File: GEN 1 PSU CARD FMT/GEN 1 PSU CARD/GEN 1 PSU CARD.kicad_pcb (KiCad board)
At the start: 4 copper layers, 245.3 x 107.1 mm, 15 parts, among them J2 1935226, J3 1935226, J4 39-28-1243, U1 ProMicro

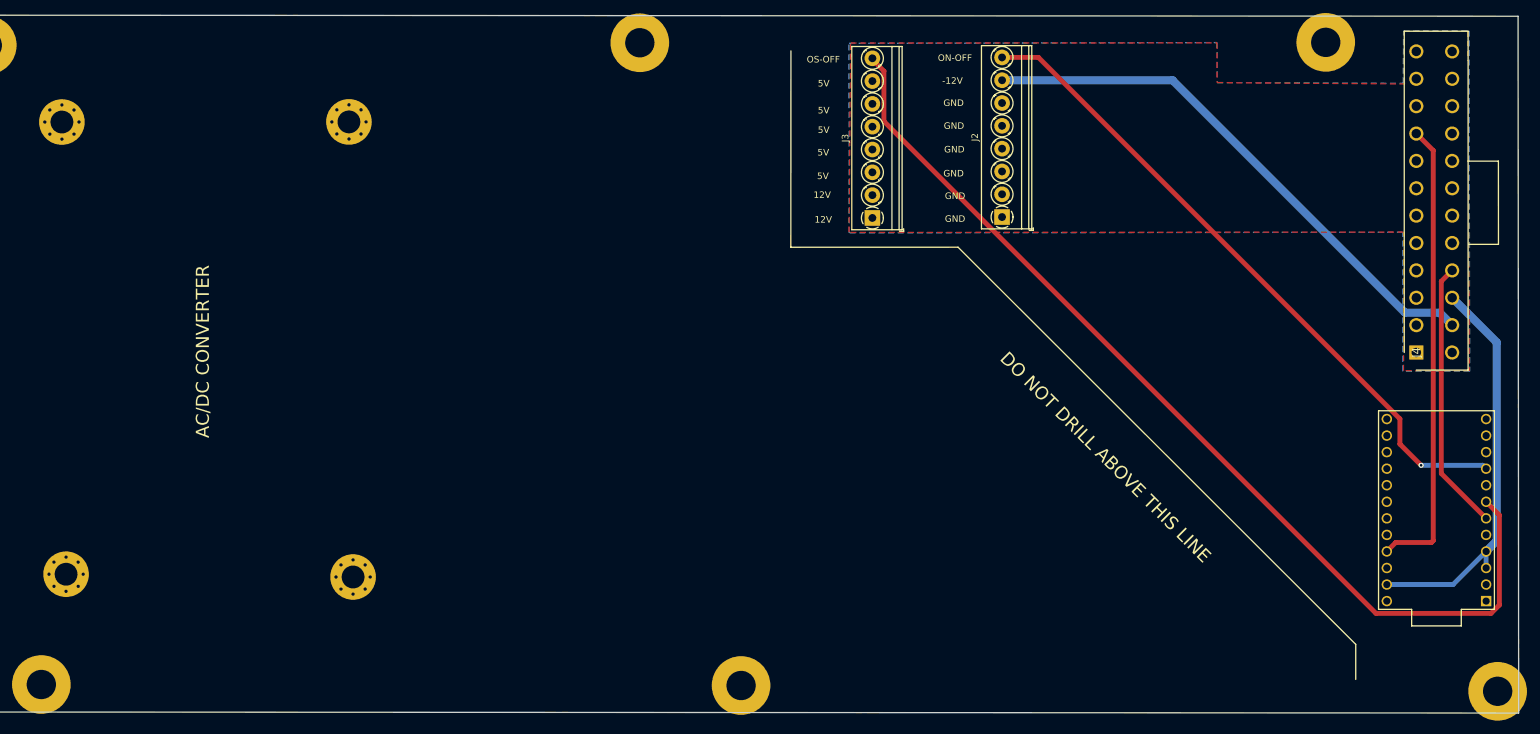
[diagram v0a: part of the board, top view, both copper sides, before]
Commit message: Gen 1 Card update
-Revised Gen1 card and added high power ACDC converter footprint and repositioned components so it's two layer.
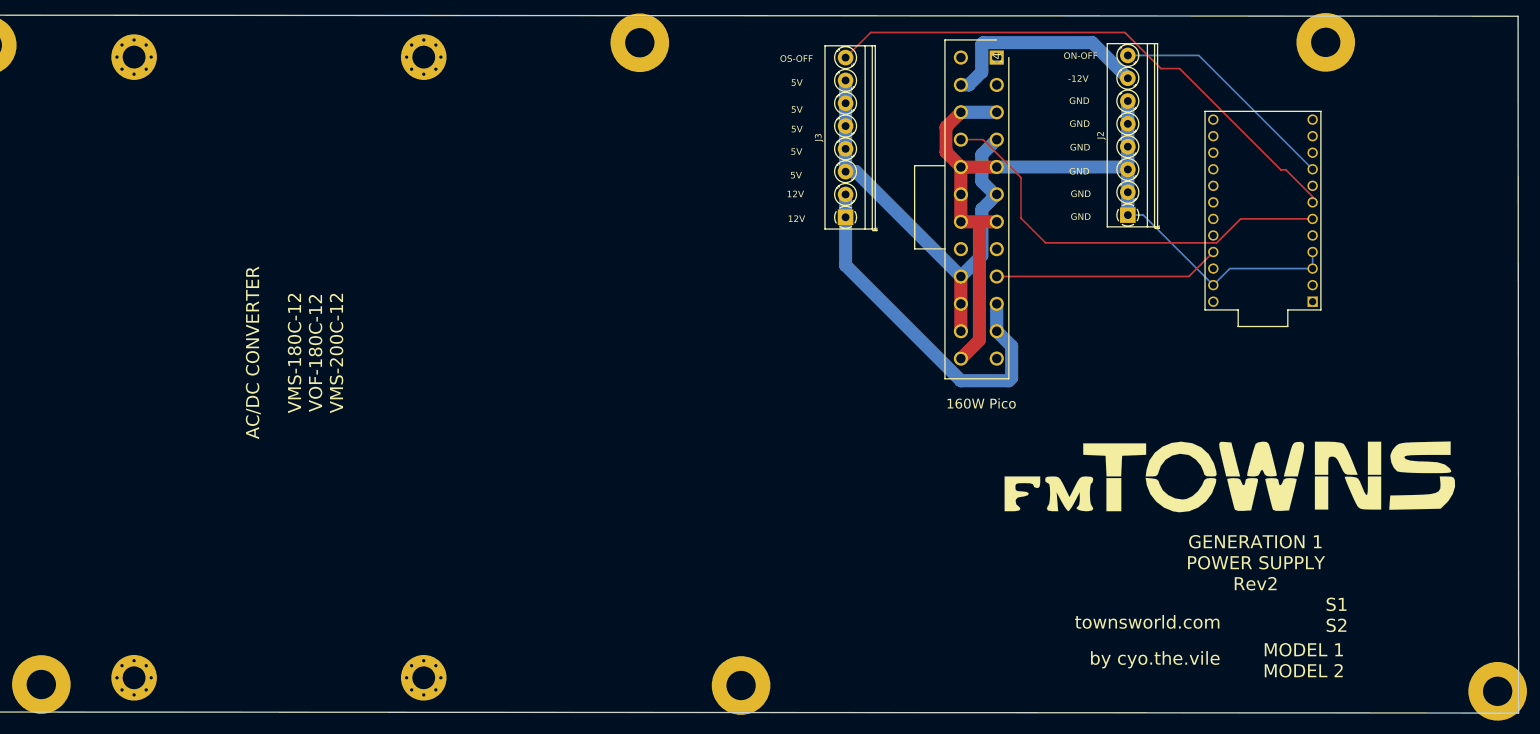
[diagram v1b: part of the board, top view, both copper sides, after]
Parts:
- G***: moved to F.Cu
- moved G*** 88.4 mm to (224.8, 116.1), turned to 0 degrees
- moved REF** 86.0 mm to (56.8, 147.0), turned to 90 degrees
- moved REF** 80.5 mm to (101.2, 51.8), turned to 90 degrees
- moved J4 78.7 mm to (189.2, 51.8), turned to 270 degrees
- moved REF** 57.1 mm to (101.2, 147.0), turned to 90 degrees
- moved U1 53.1 mm to (230.0, 75.3)
- moved REF** 34.4 mm to (56.8, 51.8), turned to 90 degrees
- moved J2 19.3 mm to (209.3, 76.0)
- moved J3 4.12 mm to (166.0, 76.4)
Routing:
- net /5V: track 0.00 -> 72.1 mm
- net /GND: track 62.3 -> 131.5 mm
- net /OS_OFF: track 153.4 -> 84.6 mm
- net /ON-OFF: track 102.7 -> 35.6 mm, vias 1 -> 0
- net /12V: track 0.00 -> 56.2 mm
- net /-12: track 84.6 -> 33.1 mm
- net /5VSB: track 71.4 -> 34.8 mm
- net /PS_ON: track 41.6 -> 65.7 mm
- removed copper zone on Layer3, net /12V
- removed copper zone on Layer2, net /5V
- removed copper zone on B.Cu, net /GND
- removed copper zone on F.Cu, net /GND
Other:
- copper layers 4 -> 2
- board text added: "160W Pico"
- board text added: "AC/DC CONVERTER VMS-180C-12 VOF-180C-12 VMS-200C-12"
- board text added: "GENERATION 1 POWER SUPPLY Rev2"
- board text removed: "AC/DC CONVERTER"
- board text removed: "DO NOT DRILL ABOVE THIS LINE"
- board text removed: "GENERATION 1 POWER SUPPLY"

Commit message: Update
Updated Rev2
Now 2 Layer card
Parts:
- removed the REF** at (266.0, 149.1)
- removed the REF** at (239.7, 49.5)
- G***: moved to B.Cu
- moved G*** 146.9 mm to (80.4, 89.1), turned to 180 degrees
- moved U1 91.9 mm to (138.9, 87.7)
- moved REF** 0.76 mm to (149.9, 147.4)
- moved REF** 0.63 mm to (134.4, 50.2)
- moved REF** 0.61 mm to (42.6, 147.4)
- moved REF** 0.24 mm to (34.3, 50.2)
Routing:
- net /ON-OFF: track 35.6 -> 86.6 mm
- net /OS_OFF: track 84.6 -> 45.9 mm
- net /5VSB: track 34.8 -> 61.4 mm, vias 0 -> 1
- net /GND: track 131.5 -> 154.0 mm
- net /PS_ON: track 65.7 -> 52.1 mm, vias 0 -> 1
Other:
- board size 245.3 x 107.1 mm -> 190.9 x 107.1 mm
